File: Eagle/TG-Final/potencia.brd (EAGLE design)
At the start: 160 x 110 mm, 34 parts, among them IC1 7812T, Q1 2N3055, T1 2N3904

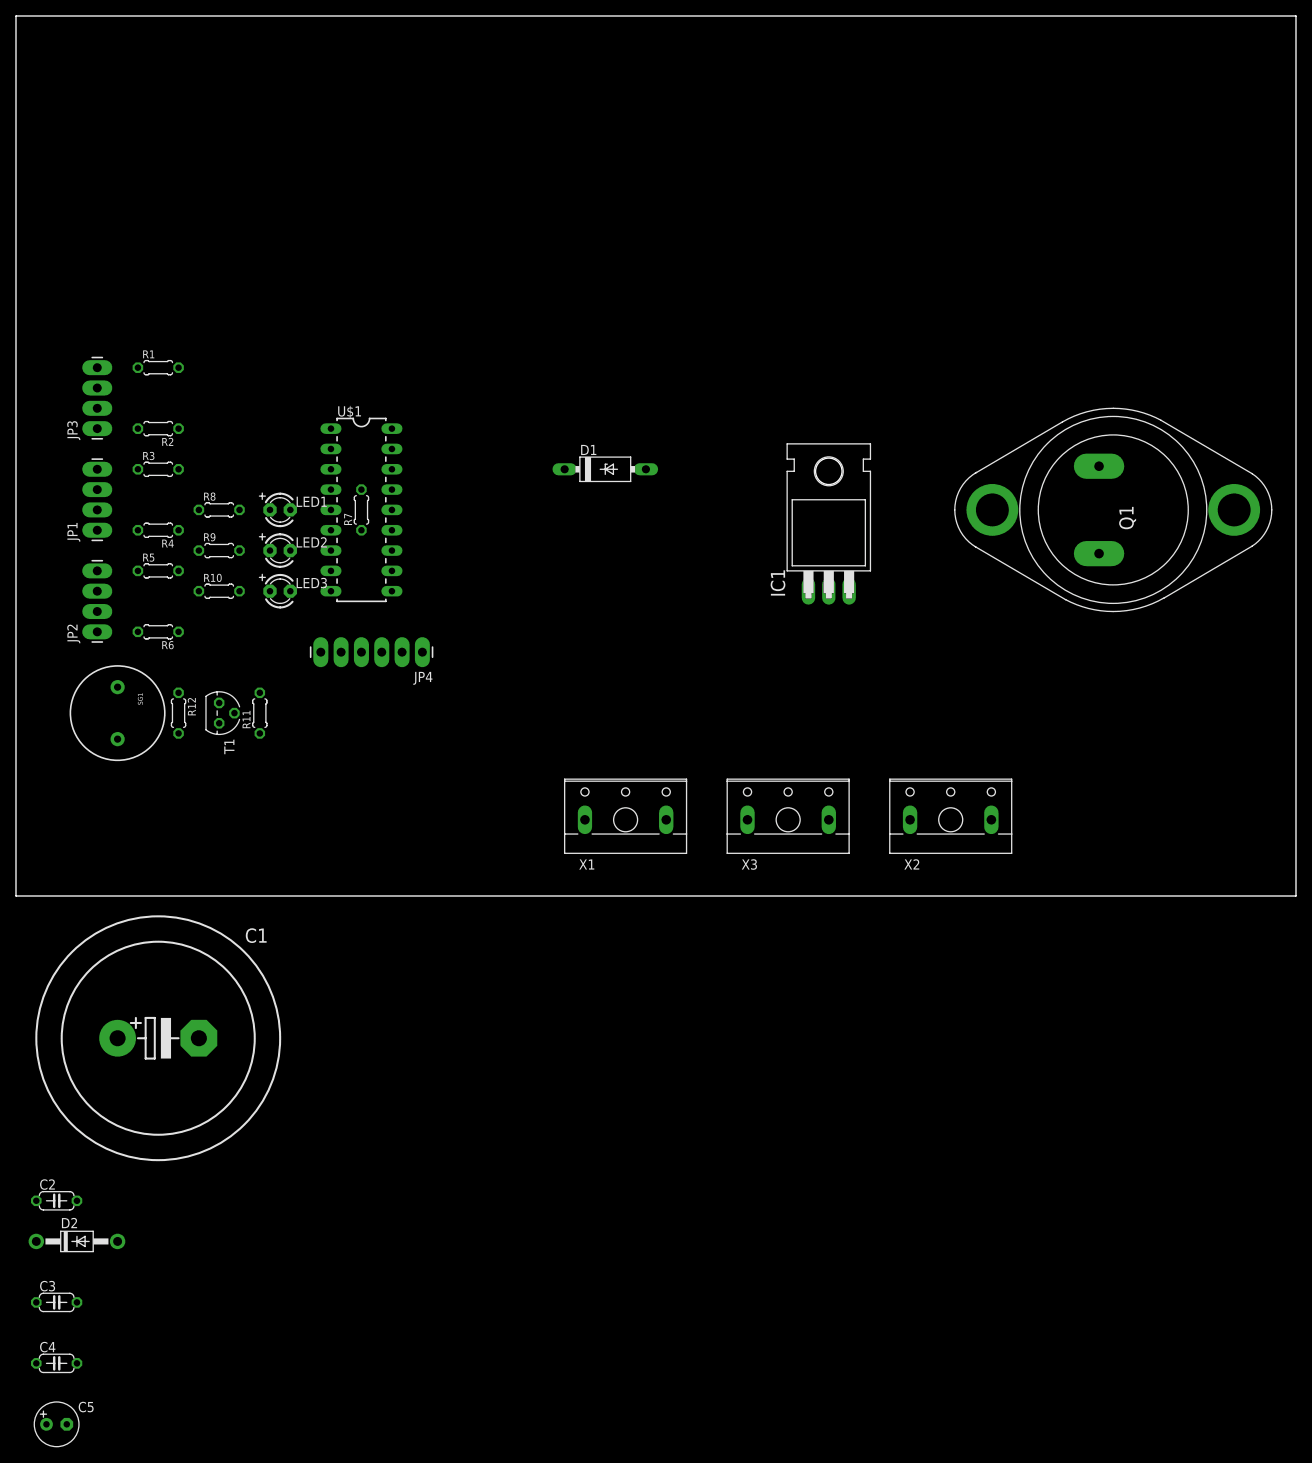
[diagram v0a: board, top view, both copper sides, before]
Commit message: Esquematicos para placa logica
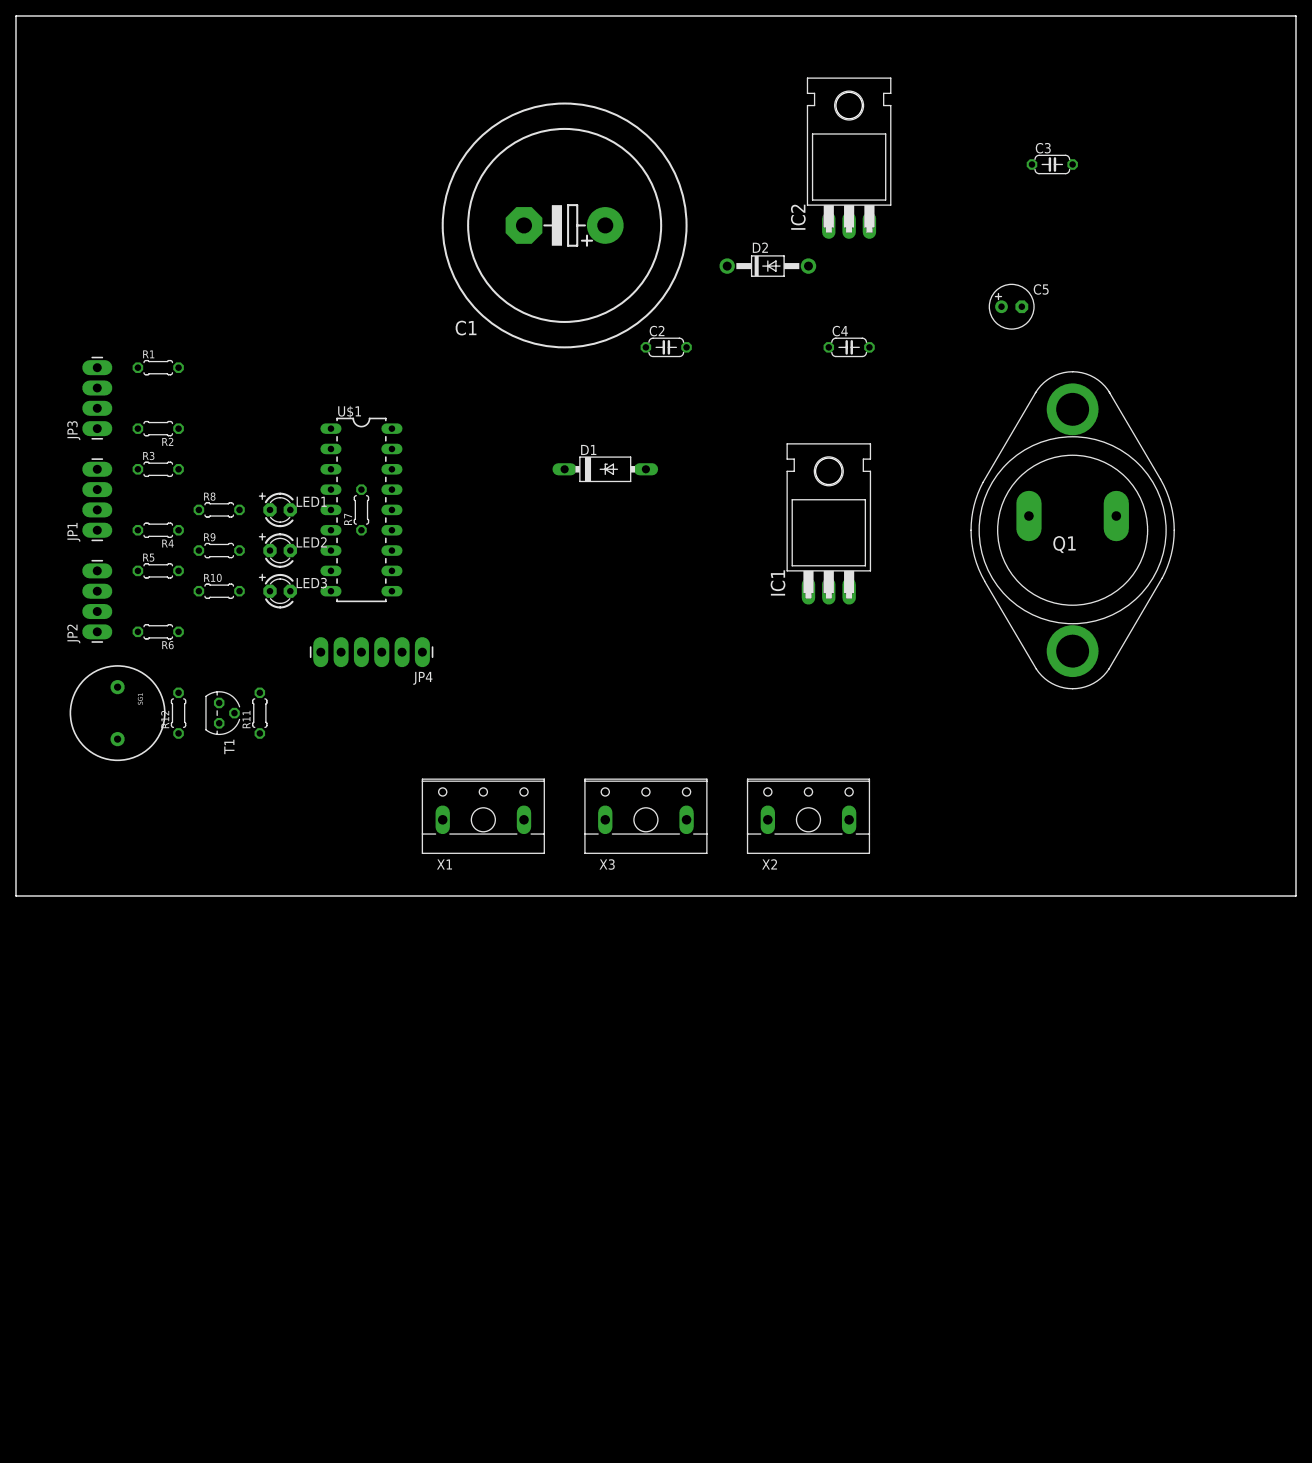
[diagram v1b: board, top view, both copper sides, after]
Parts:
- added IC2: 7805T, adafruit:TO220H
- moved C3 189.0 mm to (129.5, 91.4)
- moved C5 183.8 mm to (124.5, 73.7)
- moved C4 161.1 mm to (104.1, 68.6)
- moved D2 149.4 mm to (94.0, 78.7)
- moved C2 131.1 mm to (81.3, 68.6)
- moved C1 113.6 mm to (68.6, 83.8), turned to 180 degrees
- moved X1 17.8 mm to (58.4, 10.2)
- moved X2 17.8 mm to (99.1, 10.2)
- moved X3 17.8 mm to (78.7, 10.2)
- moved Q1 5.68 mm to (132.1, 45.7), turned to 270 degrees
- turned R12 to 90 degrees
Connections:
- new net N$23: IC2.1, X1.1
